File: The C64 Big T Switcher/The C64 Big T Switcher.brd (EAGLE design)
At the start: 62.2 x 63.5 mm, 6 parts, among them IC1 C64 ROM SOCKET, IC2 27256 EEPROM, J1 C64, J2 PLED, U1 ATTINY85

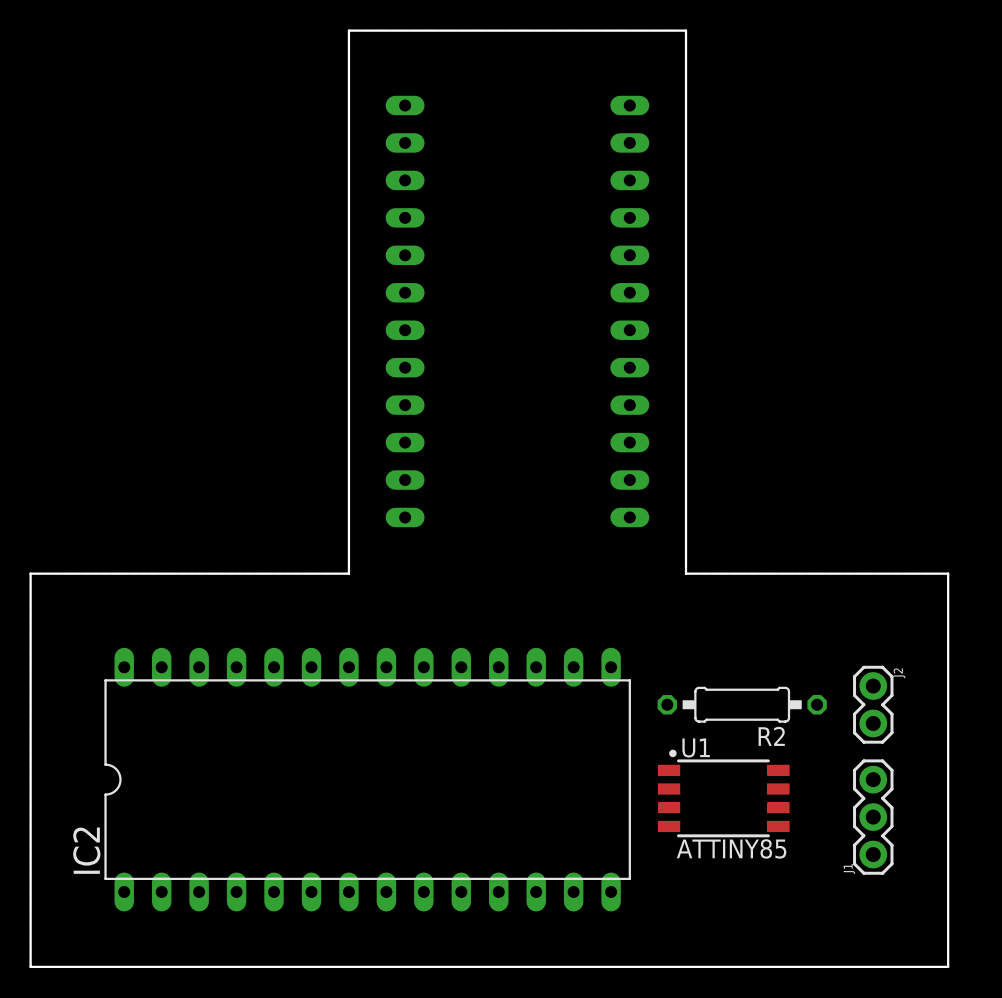
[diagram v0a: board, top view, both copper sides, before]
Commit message: Renamed Rom Selector (ATTiny85) to Big T Switcher
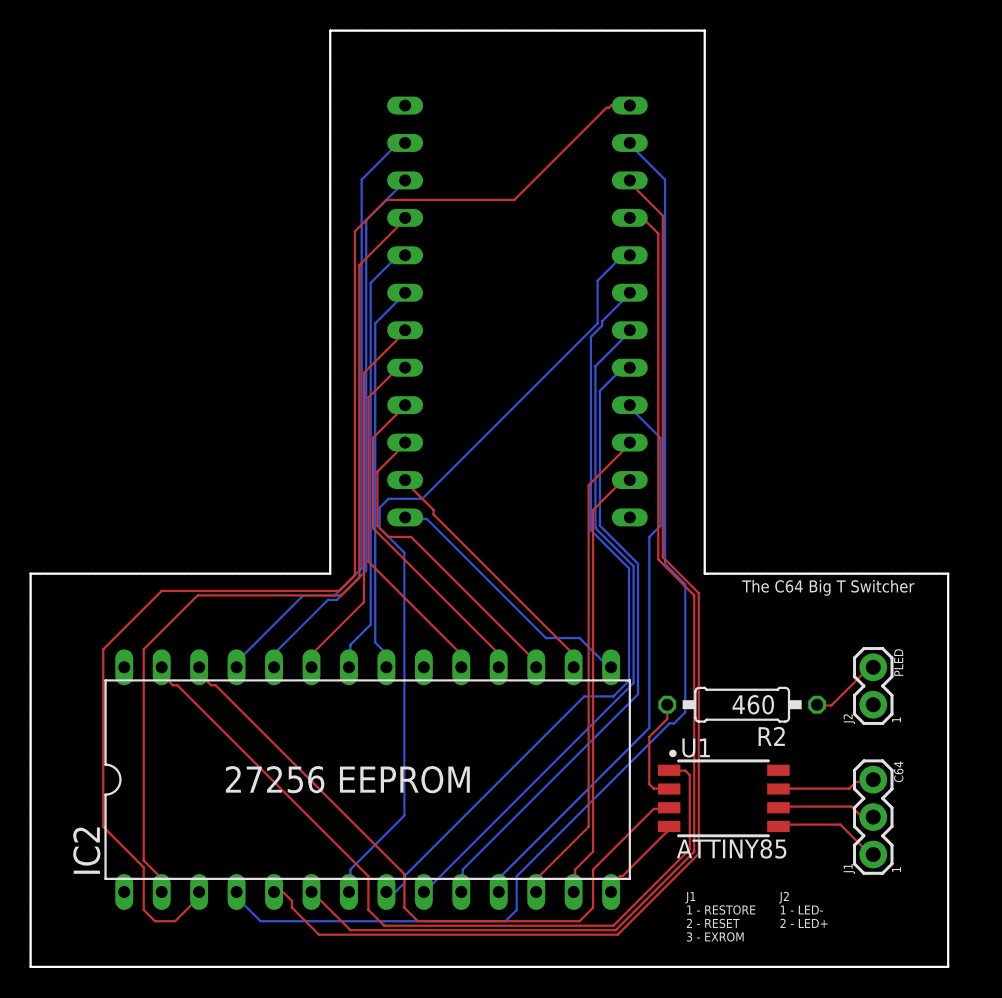
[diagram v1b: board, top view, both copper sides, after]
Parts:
- moved J2 1.27 mm to (55.9, 16.5), turned to 90 degrees
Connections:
- net PIN1 renamed RESTORE
- net PIN2 renamed RESET
- net PIN3 renamed EXROM
- net PIN4 renamed PLED
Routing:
- net A7: track 0.00 -> 88.6 mm
- net A5: track 0.00 -> 80.2 mm
- net A6: track 0.00 -> 78.9 mm
- net A4: track 0.00 -> 74.5 mm
- net A12: track 0.00 -> 59.4 mm
- net A3: track 0.00 -> 54.1 mm
- net A14: track 0.00 -> 53.4 mm
- net A2: track 0.00 -> 51.1 mm
- net A1: track 0.00 -> 46.2 mm
- net A13: track 0.00 -> 45.3 mm
- net A0: track 0.00 -> 42.8 mm
- net A8: track 0.00 -> 41.9 mm
- net D0: track 0.00 -> 38.5 mm
- net A9: track 0.00 -> 37.1 mm
- net D1: track 0.00 -> 33.3 mm
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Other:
- outline, holes or cut-outs redrawn
- board text added: "1"
- board text added: "J1 1 - RESTORE 2 - RESET 3 - EXROM"
- board text added: "J2 1 - LED- 2 - LED+"
- board text added: "The C64 Big T Switcher"
